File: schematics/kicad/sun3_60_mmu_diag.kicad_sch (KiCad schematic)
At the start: 26 parts, among them J200 DIAG, U200 7188, U201 7188, U202 2168, U203 2168, U205 2168, U206 2168, U207 2168, U208 2168, U210 LS2518, U212 ALS245, U213 ALS245, U215 ALS245, U217 ALS245, U218 ALS245, U223 74F534, U224 AM27S19, U225 ALS273, U226 ALS373, U227 ALS273, U228 LED_Block, U229 LED_Block, U230 PAL16L8, U231 PAL16L8, U232 PAL16L8

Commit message: First draft for an expanded MMU
This version uses vintage parts except for the SRAM, which are IS61C5128AS-25HLI (they could be QLI instead)
Unfortunately, this requires:
* 2 more 74ALS245 to buffer the second byte of PMAP indices in the SMAP
* one more LS2518 (!) to extend the context register
* a couple of 74CBTLV3257 to be able to stay in "normal" Sun3 mode with minimal delays on the signals
* a couple of switches to enabled/disable the new features
* some extra passives
* U231, a PAL16L8, needs another input and another two outputs, or can be split in two PALs (or GAL, CPLDs, ...)

Also this does not include tne necessary decoupling on the new components
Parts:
- removed J200: DIAG, Connector_PinHeader_2.54mm:PinHeader_1x03_P2.54mm_Vertical, symbol Switch:SW_Push_SPDT
- removed U200, U201: 7188, sun3_60:7188, symbol custom:7188
- removed U202, U203, U205, U206, U207, U208: 2168, sun3_60:2168, symbol custom:2168
- added R1, R2, R3, R4, R5: 10k, symbol Device:R
- added S3: 4.7k Ohm, Resistor_THT:R_Array_SIP10, symbol Device:R_Network09
- added SW1, SW2: SW_SPDT, symbol Switch:SW_SPDT
- added U1, U2, U3, U4, U7, U8: IS61C5128AS-25HLI, Package_SO:TSOP-I-32_11.8x8mm_P0.5mm, symbol Memory_RAM:IS61C5128AS-25HLI
- added U10, U11: 74CBTLV3257, symbol 74xx:74CBTLV3257
- added U5, U6: ALS245, sun3_60:ALS245, symbol custom:ALS245
- added U9: LS2518, sun3_60:LS2518, symbol custom:LS2518
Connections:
- net A13: now also U1.20 (A0), U2.20 (A0), U3.20 (A0), U4.20 (A0)
- net A14: now also U1.19 (A1), U2.19 (A1), U3.19 (A1), U4.19 (A1)
- net A15: now also U1.18 (A2), U2.18 (A2), U3.18 (A2), U4.18 (A2)
- net A16: now also U1.17 (A3), U2.17 (A3), U3.17 (A3), U4.17 (A3)
- net A17: now also U7.14 (A6), U8.14 (A6)
- net A18: now also U7.13 (A7), U8.13 (A7)
- net A19: now also U7.3 (A8), U8.3 (A8)
- net A20: now also U7.2 (A9), U8.2 (A9)
- net A21: now also U7.31 (A10), U8.31 (A10)
- net A22: now also U7.1 (A11), U8.1 (A11)
- net A23: now also U7.12 (A12), U8.12 (A12)
- net A24: now also U7.4 (A13), U8.4 (A13)
- net A25: now also U7.11 (A14), U8.11 (A14)
- net A26: now also U7.7 (A15), U8.7 (A15)
- net A27: now also U7.10 (A16), U8.10 (A16)
- net A28: now also U10.5
- net A30: now also U10.2
- net ACCESS: now also U3.23 (I/O2)
- net CX0: now also U7.20 (A0), U8.20 (A0)
- net CX1: now also U7.19 (A1), U8.19 (A1)
- net CX2: now also U7.18 (A2), U8.18 (A2)
- net EN.CTL-: now also U11.2
- net GND: now also R2.1, R3.1, R5.1, S3.1 (common), U1.24 (GND), U1.32 (~{OE}), U10.10, U10.13, U10.14, U10.15 (~{OE}), U10.3, U10.6, U10.8 (GND), U11.15 (~{OE}), U11.8 (GND), U2.24 (GND), U2.32 (~{OE}), U3.24 (GND), U3.32 (~{OE}), U4.24 (GND), U4.32 (~{OE}), U5.10 (GND), U6.10 (GND), U7.32 (~{OE}), U8.24 (GND), U8.32 (~{OE}), U9.8 (GND)
- net MMU.S: now also U4.23 (I/O2)
- net MMU.V: now also U4.21 (I/O0)
- net MMU.W: now also U4.22 (I/O1)
- net MMU.X: now also U4.25 (I/O3)
- net MMU0: now also U5.2 (A0), U6.18 (B0)
- net MMU1: now also U5.3 (A1), U6.17 (B1)
- net MMU2: now also U5.4 (A2), U6.16 (B2)
- net MMU3: now also U5.5 (A3), U6.15 (B3)
- net MMU4: now also U5.6 (A4), U6.14 (B4), U9.1 (D0), U9.3 (Y0)
- net MMU5: now also U5.7 (A5), U6.13 (B5), U9.4 (D1), U9.6 (Y1)
- net MMU6: now also U5.8 (A6), U6.12 (B6), U9.10 (Y2), U9.12 (D2)
- net MMU7: now also U5.9 (A7), U6.11 (B7), U9.13 (Y3), U9.15 (D3)
- net MODIFY: now also U3.25 (I/O3)
- net PA13: now also U1.21 (I/O0)
- net PA14: now also U1.22 (I/O1)
- net PA15: now also U1.23 (I/O2)
- net PA16: now also U1.25 (I/O3)
- net PA17: now also U1.26 (I/O4)
- net PA18: now also U1.27 (I/O5)
- net PA19: now also U1.28 (I/O6)
- net PA20: now also U1.29 (I/O7)
- net PA21: now also U2.21 (I/O0)
- net PA22: now also U2.22 (I/O1)
- net PA23: now also U2.23 (I/O2)
- net PA24: now also U2.25 (I/O3)
- net PA25: now also U2.26 (I/O4)
- net PA26: now also U2.27 (I/O5)
- net PA27: now also U2.28 (I/O6)
- net PA28: now also U2.29 (I/O7)
- net PD0-: now also U7.30 (~{CE}), U8.30 (~{CE})
- net PD1-: now also U1.30 (~{CE}), U2.30 (~{CE}), U3.30 (~{CE}), U4.30 (~{CE})
- net RD.CX-: now also U9.7 (OE-)
- net READ-: now also U5.1 (A->B), U6.1 (A->B)
- net SA17: now also U1.16 (A4), U2.16 (A4), U3.16 (A4), U4.16 (A4), U7.21 (I/O0)
- net SA18: now also U1.15 (A5), U2.15 (A5), U3.15 (A5), U4.15 (A5), U7.22 (I/O1)
- net SA19: now also U1.14 (A6), U2.14 (A6), U3.14 (A6), U4.14 (A6), U7.23 (I/O2)
- net SA20: now also U1.13 (A7), U2.13 (A7), U3.13 (A7), U4.13 (A7), U7.25 (I/O3)
- net SA21: now also U1.3 (A8), U2.3 (A8), U3.3 (A8), U4.3 (A8), U7.26 (I/O4)
- net SA22: now also U1.2 (A9), U2.2 (A9), U3.2 (A9), U4.2 (A9), U7.27 (I/O5)
- net SA23: now also U1.31 (A10), U2.31 (A10), U3.31 (A10), U4.31 (A10), U7.28 (I/O6)
- net SA24: now also U1.1 (A11), U2.1 (A11), U3.1 (A11), U4.1 (A11), U7.29 (I/O7)
- net TYPE0: now also U3.22 (I/O1)
- net TYPE1: now also U3.21 (I/O0)
- net VCC: now also R1.1, R4.1, U1.8 (VDD), U10.16 (VCC), U11.10, U11.13, U11.16 (VCC), U11.3, U11.6, U2.8 (VDD), U3.8 (VDD), U4.8 (VDD), U5.20 (VCC), U6.20 (VCC), U7.8 (VDD), U8.8 (VDD), U9.16 (VCC)
- net WE.PMAP0-: now also U4.5 (~{WE})
- net WE.PMAP2-: now also U2.5 (~{WE})
- net WE.PMAP3-: now also U1.5 (~{WE})
- net WE.SMAP-: now also U7.5 (~{WE})
- net WE.STAT-: now also U3.5 (~{WE})
- net WR.CX-: now also U11.14
- net CX3: now reaches U210.14 (Q3)
- net CX3: now also R3.2, U11.11
- new net: R4.2, SW2.3 (C)
- new net: R5.2, SW2.1 (A)
- new net: S3.2 (R1), U5.18 (B0)
- new net: R2.2, SW1.1 (A)
- new net: R1.2, SW1.3 (C)
- new net CX4: U7.16 (A4), U8.16 (A4), U9.2 (Q0)
- new net CX5: U7.15 (A5), U8.15 (A5), U9.5 (Q1)
- new net D16: U6.2 (A0)
- new net D17: U6.3 (A1)
- new net D18: U6.4 (A2)
- new net D19: U6.5 (A3)
- new net D20: U6.6 (A4)
- new net D21: U6.7 (A5)
- new net D22: U6.8 (A6)
- new net D23: U6.9 (A7)
- new net EN.SMAP1-: U11.5
- new net ENABLE_S3E: SW1.2 (B), U11.1 (S)
- new net ENABLE_S3E_V: SW2.2 (B), U10.1 (S)
- new net S3E_A28: U10.7, U7.9 (A17), U8.9 (A17)
- new net S3E_A30: U10.4, U7.6 (A18), U8.6 (A18)
- new net S3E_CX3: U11.9, U7.17 (A3), U8.17 (A3)
- new net S3E_EN.CTL-: U11.4, U6.19 (CE)
- new net S3E_EN.SMAP1-: U11.7, U5.19 (CE)
- new net S3E_WR.CX-: U11.12, U9.9 (CP)
- new net SA25: S3.3 (R2), U1.12 (A12), U2.12 (A12), U3.12 (A12), U4.12 (A12), U5.17 (B1), U8.21 (I/O0)
- new net SA26: S3.4 (R3), U1.4 (A13), U2.4 (A13), U3.4 (A13), U4.4 (A13), U5.16 (B2), U8.22 (I/O1)
- new net SA27: S3.5 (R4), U1.11 (A14), U2.11 (A14), U3.11 (A14), U4.11 (A14), U5.15 (B3), U8.23 (I/O2)
- new net SA28: S3.6 (R5), U1.7 (A15), U2.7 (A15), U3.7 (A15), U4.7 (A15), U5.14 (B4), U8.25 (I/O3)
- new net SA29: S3.7 (R6), U1.10 (A16), U2.10 (A16), U3.10 (A16), U4.10 (A16), U5.13 (B5), U8.26 (I/O4)
- new net SA30: S3.8 (R7), U1.9 (A17), U2.9 (A17), U3.9 (A17), U4.9 (A17), U5.12 (B6), U8.27 (I/O5)
- new net SA31: S3.9 (R8), U1.6 (A18), U2.6 (A18), U3.6 (A18), U4.6 (A18), U5.11 (B7), U8.28 (I/O6)
- new net WE.SMAP1-: U8.5 (~{WE})
- no-connect marks 3 -> 14
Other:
- note added: "CONTEXT (cx3 added with pull-down)"
- note added: "CONTEXT (upper nybble) Context register is accessed normally (byte), just with a different mask Normal Sun3 is CtxId & 0x7 (3 bits) Extended Sun3 is CtxId & 0x3f (6 bits) So we get 64 hardware contexts"
- note added: "Controls for additional input signals. S3E_* are 'filtered' version of the normal signal. When ENABLE_S3E is unwanted, then the additional chips are always disabled and all additional address lines to the PMAP and SPMAP SRAMs are zero. When ENABLE_S3E is wanted, the additional chips track the behavior of those they extend. exnteded virtual memory (ENABLE_S3E is handled separately to ease debug), 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"
- note added: "Order of address bits can change"
- note added: "Second byte of segment index. Uses aligned load/store word *shifted left by one* instead of load/store byte for value of PMAP index D16 is not actually stored or used, so only the upper 15 bits of the word are meaningful. PLEASE NOTE: The MMU bus is only wired for 8 bits not matter what; the design of the 3/60 rely on the MC68020 bus sizing properties to work. For instance, when doing a LONG acce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"
- note added: "Switch / pull-up/down form factors TBD"
- note added: "U202"
- note added: "U203"
- note added: "U205/U206"
- note added: "U207/U208"
- note added: "U231 needs a bigger PAL (or two PALs) (a) it needs to output EN.SMAP1- & WE.SMAP1- WE_SMAP = ( !A28 & A29 & !A30 & EN_CTL & WRITE & C_S3 & !C_S7X); EN_SMAP = ( !A28 & A29 & !A30 & EN_CTL & C_S5); (which ignore alignement) should become /* byte or upper byte of word */ WE_SMAP = (!A1 & !A0 & !A28 & A29 & !A30 & EN_CTL & WRITE & C_S3 & !C_S7X); EN_SMAP = (!A1 & !A0 & !A28 & A29 & !A30 & EN_CTL & C_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"
- note added: "order of data bits can change inside each SRAM."
- note removed: "CONTEXT"

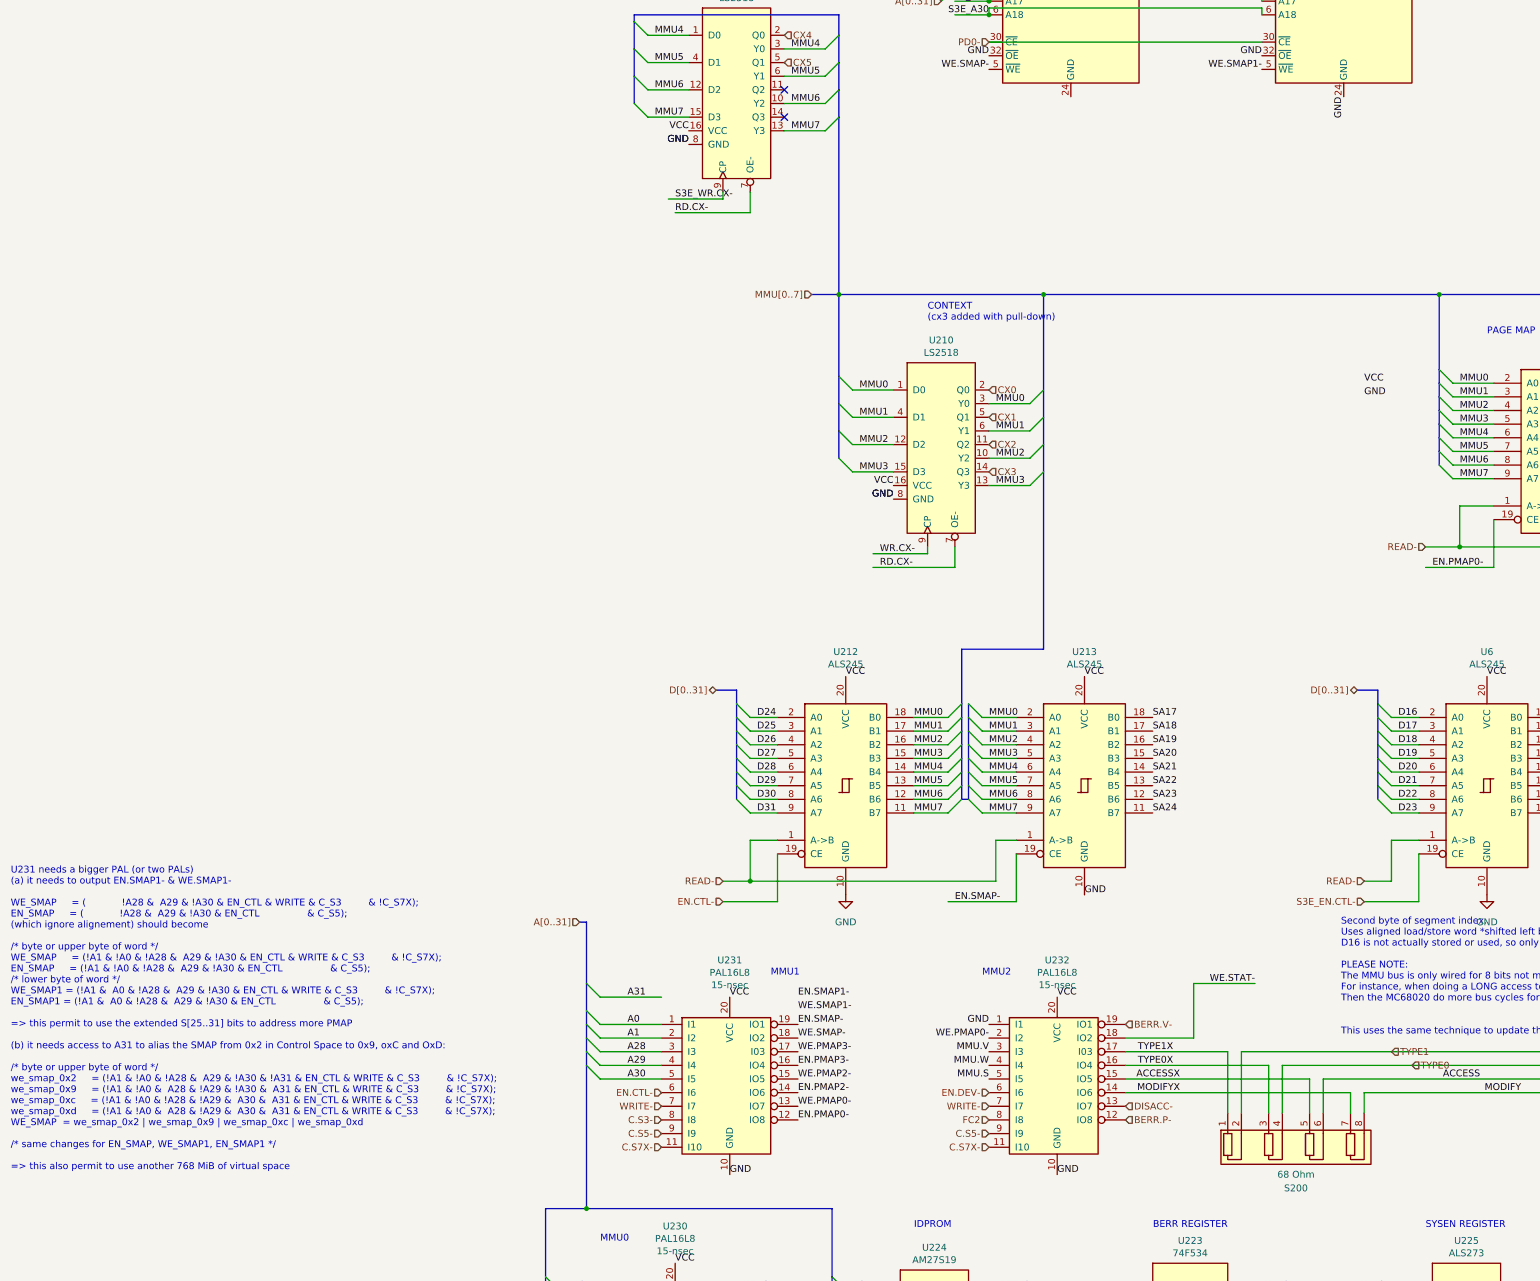
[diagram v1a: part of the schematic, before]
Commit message: PMAP1, missing GND
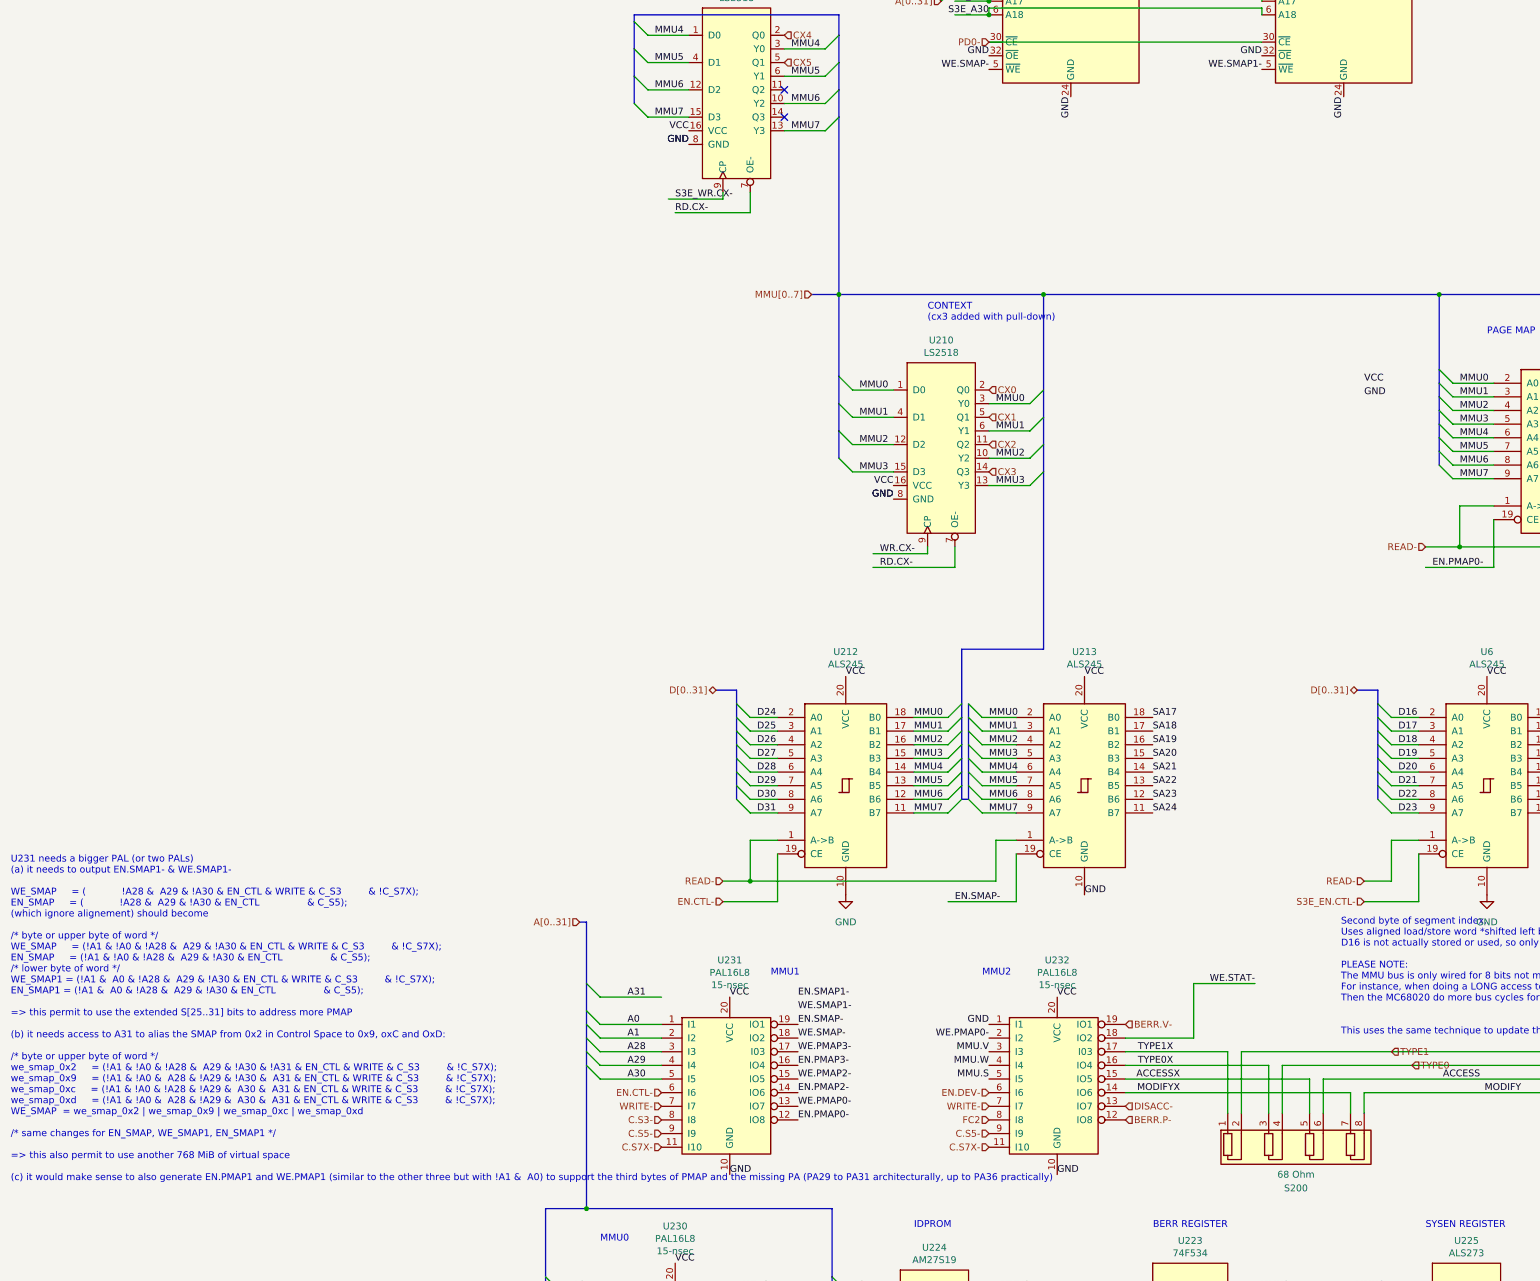
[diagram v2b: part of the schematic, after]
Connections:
- net GND: now also U7.24 (GND)
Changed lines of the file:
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@@
 		)
 	)
-	(text "U231 needs a bigger PAL (or two PALs)\n(a) it needs to output EN.SMAP1- & WE.SMAP1-\n\nWE_SMAP	 = (            !A28 &  A29 & !A30 & EN_CTL & WRITE & C_S3         & !C_S7X);\nEN_SMAP	 = (            !A28 &  A29 & !A30 & EN_CTL                & C_S5);\n(which ignore alignement) should become\n\n/* byte or upper byte of word */\nWE_SMAP	 = (!A1 & !A0 & !A28 &  A29 & !A30 & EN_CTL & WRITE & C_S3         & !C_S7X);\nEN_SMAP	 = (!A1 & !A0 & !A28 &  A29 & !A30 & EN_CTL                & C_S5);\n/* lower byte of word */\nWE_SMAP1 = (!A1 &  A0 & !A28 &  A29 & !A30 & EN_CTL & WRITE & C_S3         & !C_S7X);\nEN_SMAP1 = (!A1 &  A0 & !A28 &  A29 & !A30 & EN_CTL                & C_S5);\n\n=> this permit to use the extended S[25..31] bits to address more PMAP\n\n(b) it needs access to A31 to alias the SMAP from 0x2 in Control Space to 0x9, oxC and OxD:\n\n/* byte or upper byte of word */\nwe_smap_0x2	 = (!A1 & !A0 & !A28 &  A29 & !A30 & !A31 & EN_CTL & WRITE & C_S3         & !C_S7X);\nwe_smap_0x9	 = (!A1 & !A0 &  A28 & !A29 & !A30 &  A31 & EN_CTL & WRITE & C_S3         & !C_S7X);\nwe_smap_0xc	 = (!A1 & !A0 & !A28 & !A29 &  A30 &  A31 & EN_CTL & WRITE & C_S3         & !C_S7X);\nwe_smap_0xd	 = (!A1 & !A0 &  A28 & !A29 &  A30 &  A31 & EN_CTL & WRITE & C_S3         & !C_S7X);\nWE_SMAP  = we_smap_0x2 | we_smap_0x9 | we_smap_0xc | we_smap_0xd\n\n/* same changes for EN_SMAP, WE_SMAP1, EN_SMAP1 */\n\n=> this also permit to use another 768 MiB of virtual space"
+	(text "U231 needs a bigger PAL (or two PALs)\n(a) it needs to output EN.SMAP1- & WE.SMAP1-\n\nWE_SMAP	 = (            !A28 &  A29 & !A30 & EN_CTL & WRITE & C_S3         & !C_S7X);\nEN_SMAP	 = (            !A28 &  A29 & !A30 & EN_CTL                & C_S5);\n(which ignore alignement) should become\n\n/* byte or upper byte of word */\nWE_SMAP	 = (!A1 & !A0 & !A28 &  A29 & !A30 & EN_CTL & WRITE & C_S3         & !C_S7X);\nEN_SMAP	 = (!A1 & !A0 & !A28 &  A29 & !A30 & EN_CTL                & C_S5);\n/* lower byte of word */\nWE_SMAP1 = (!A1 &  A0 & !A28 &  A29 & !A30 & EN_CTL & WRITE & C_S3         & !C_S7X);\nEN_SMAP1 = (!A1 &  A0 & !A28 &  A29 & !A30 & EN_CTL                & C_S5);\n\n=> this permit to use the extended S[25..31] bits to address more PMAP\n\n(b) it needs access to A31 to alias the SMAP from 0x2 in Control Space to 0x9, oxC and OxD:\n\n/* byte or upper byte of word */\nwe_smap_0x2	 = (!A1 & !A0 & !A28 &  A29 & !A30 & !A31 & EN_CTL & WRITE & C_S3         & !C_S7X);\nwe_smap_0x9	 = (!A1 & !A0 &  A28 & !A29 & !A30 &  A31 & EN_CTL & WRITE & C_S3         & !C_S7X);\nwe_smap_0xc	 = (!A1 & !A0 & !A28 & !A29 &  A30 &  A31 & EN_CTL & WRITE & C_S3         & !C_S7X);\nwe_smap_0xd	 = (!A1 & !A0 &  A28 & !A29 &  A30 &  A31 & EN_CTL & WRITE & C_S3         & !C_S7X);\nWE_SMAP  = we_smap_0x2 | we_smap_0x9 | we_smap_0xc | we_smap_0xd\n\n/* same changes for EN_SMAP, WE_SMAP1, EN_SMAP1 */\n\n=> this also permit to use another 768 MiB of virtual space\n\n(c) it would make sense to also generate EN.PMAP1 and WE.PMAP1 (similar to the other three but with !A1 &  A0) to support the third bytes of PMAP and the missing PA (PA29 to PA31 architecturally, up to PA36 practically)"
 		(exclude_from_sim no)
 		(at -83.058 153.924 0)
@@
 		(effects
 			(font
+				(size 1.27 1.27)
+			)
+			(justify right bottom)
+		)
+	)
+	(label "GND"
+		(at 114.3 -17.78 270)
+		(effects
+			(font

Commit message: remove letofver ALS245 (data for the 2nd byte of index will come from the upper byte like evrything else) ; update comment for U231, U102 also need modifications
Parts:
- removed U6: ALS245, sun3_60:ALS245, symbol custom:ALS245
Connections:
- net EN.CTL-: no longer U11.2
- net GND: now also U10.11, U11.2, U11.3
- net VCC: no longer U11.3
- net S3E_EN.CTL-: no longer names the net of U11.4
- no-connect marks 14 -> 16

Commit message: cleanup (?)
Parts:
- added U12: ALS245, sun3_60:ALS245, symbol custom:ALS245
- added U6: IS61C5128AS-25HLI, Package_SO:TSOP-I-32_11.8x8mm_P0.5mm, symbol Memory_RAM:IS61C5128AS-25HLI
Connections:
- net A13: now also U6.20 (A0)
- net A14: now also U6.19 (A1)
- net A15: now also U6.18 (A2)
- net A16: now also U6.17 (A3)
- net GND: now also U11.10, U12.10 (GND), U6.24 (GND), U6.32 (~{OE})
- net MMU0: now also U12.2 (A0)
- net MMU1: now also U12.3 (A1)
- net MMU2: now also U12.4 (A2)
- net MMU3: now also U12.5 (A3)
- net MMU4: now also U12.6 (A4)
- net MMU5: now also U12.7 (A5)
- net MMU6: now also U12.8 (A6)
- net MMU7: now also U12.9 (A7)
- net PD1-: now also U6.30 (~{CE})
- net READ-: now also U12.1 (A->B)
- net SA17: now also U6.16 (A4)
- net SA18: now also U6.15 (A5)
- net SA19: now also U6.14 (A6)
- net SA20: now also U6.13 (A7)
- net SA21: now also U6.3 (A8)
- net SA22: now also U6.2 (A9)
- net SA23: now also U6.31 (A10)
- net SA24: now also U6.1 (A11)
- net SA25: now also U6.12 (A12)
- net SA26: now also U6.4 (A13)
- net SA27: now also U6.11 (A14)
- net SA28: now also U6.7 (A15)
- net SA29: now also U6.10 (A16)
- net SA30: now also U6.9 (A17)
- net SA31: now also U6.6 (A18)
- net VCC: now also U12.20 (VCC), U6.8 (VDD); no longer U11.10
- new net EN.PMAP1-: U12.19 (CE)
- new net PA29: U12.18 (B0), U6.21 (I/O0)
- new net PA30: U12.17 (B1), U6.22 (I/O1)
- new net PA31: U12.16 (B2), U6.23 (I/O2)
- new net PA32: U12.15 (B3), U6.25 (I/O3)
- new net PA33: U12.14 (B4), U6.26 (I/O4)
- new net PA34: U12.13 (B5), U6.27 (I/O5)
- new net PA35: U12.12 (B6), U6.28 (I/O6)
- new net PA36: U12.11 (B7), U6.29 (I/O7)
- new net WE.PMAP1-: U6.5 (~{WE})
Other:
- note added: "The 3/60 is missing the extra 3 bits PA[29..31], the upper 3 of the 19 bits comming out of the PMAP. In the PMAP, the next 5 in the same byte are reserved - let's redefine them as PA[32..36], making the maximum physical space 128 GiB :-) Disabled by default, as there's no real need for that much memory. Can be designed in/installed (along with the definition of EN.PMAP1 / WE.PMAP1 and the needed 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"
